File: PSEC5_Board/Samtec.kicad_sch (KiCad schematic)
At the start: 1 part, among them J1 QTH-040-01-X-D-DP-A

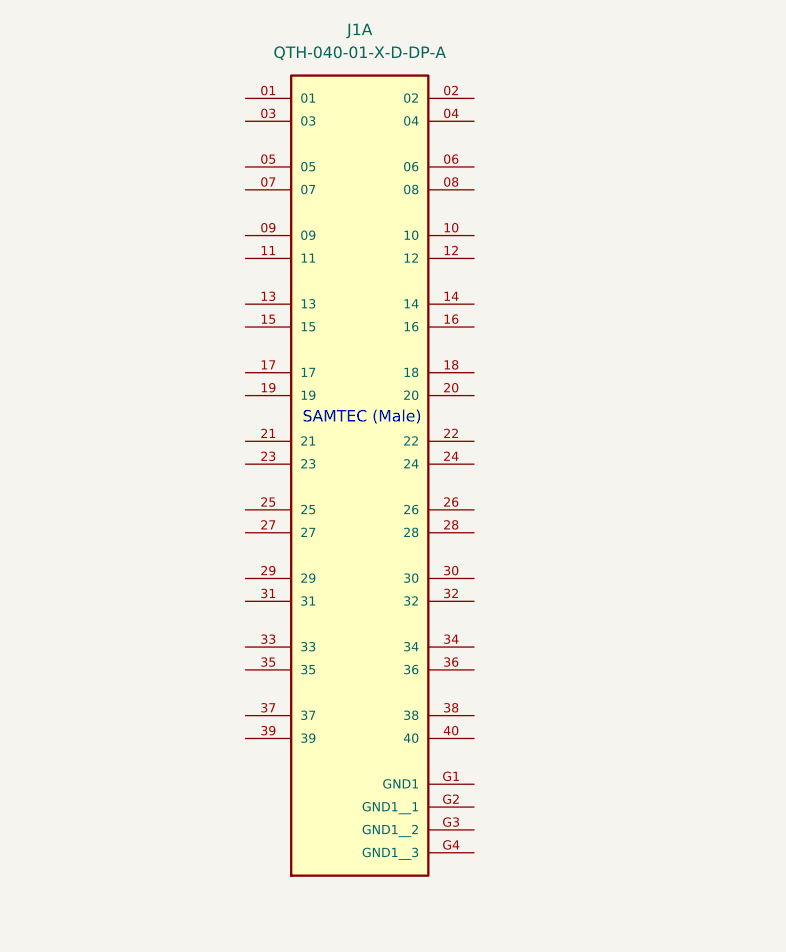
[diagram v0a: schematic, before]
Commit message: ctrl Board Schem, Updates to DUT
Uploaded all symobls for FPGA board to a ctrl_board schematic, as well as updated DUT board by adding labels to parts
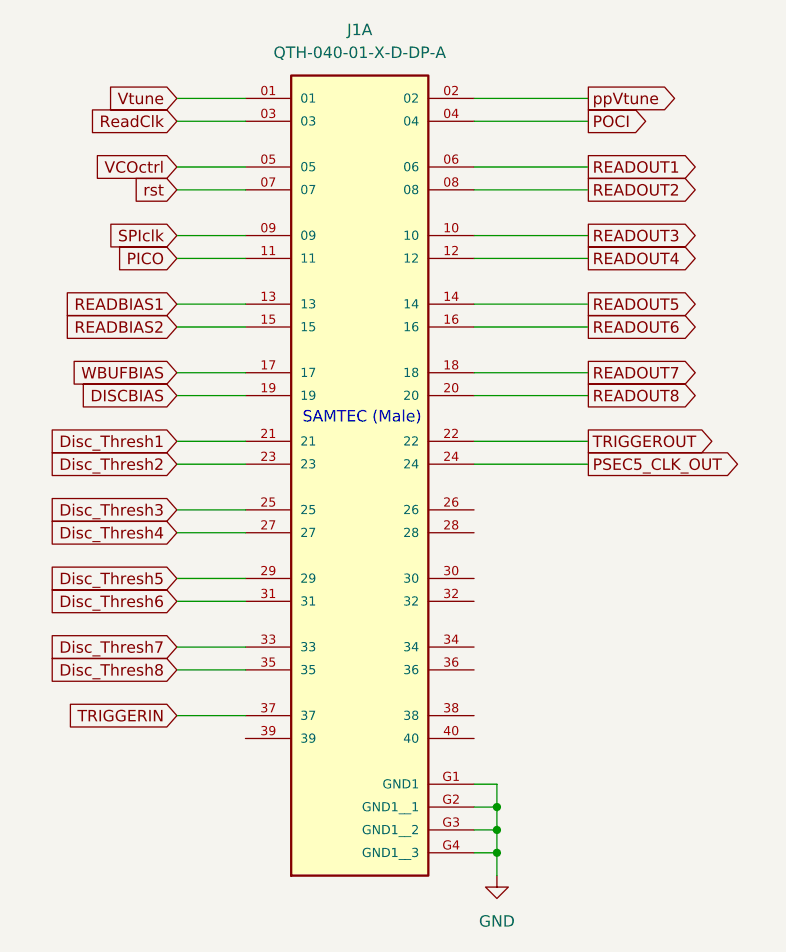
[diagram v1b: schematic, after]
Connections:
- net Vtune: now reaches J1.01
- net ppVtune: now reaches J1.02
- net ReadClk: now reaches J1.03
- net POCI: now reaches J1.04
- net VCOctrl: now reaches J1.05
- net READOUT1: now reaches J1.06
- net rst: now reaches J1.07
- net READOUT2: now reaches J1.08
- net SPIclk: now reaches J1.09
- net READOUT3: now reaches J1.10
- net PICO: now reaches J1.11
- net READOUT4: now reaches J1.12
- net READBIAS1: now reaches J1.13
- net READOUT5: now reaches J1.14
- net READBIAS2: now reaches J1.15
- net READOUT6: now reaches J1.16
- net WBUFBIAS: now reaches J1.17
- net READOUT7: now reaches J1.18
- net DISCBIAS: now reaches J1.19
- net READOUT8: now reaches J1.20
- net Disc_Thresh1: now reaches J1.21
- net TRIGGEROUT: now reaches J1.22
- net Disc_Thresh2: now reaches J1.23
- net PSEC5_CLK_OUT: now reaches J1.24
- net Disc_Thresh3: now reaches J1.25
- net Disc_Thresh4: now reaches J1.27
- net Disc_Thresh5: now reaches J1.29
- net Disc_Thresh6: now reaches J1.31
- net Disc_Thresh7: now reaches J1.33
- net Disc_Thresh8: now reaches J1.35
- net TRIGGERIN: now reaches J1.37
- net GND: now reaches J1.G1 (GND1)
- net GND: now also J1.G2 (GND1__1), J1.G3 (GND1__2), J1.G4 (GND1__3)

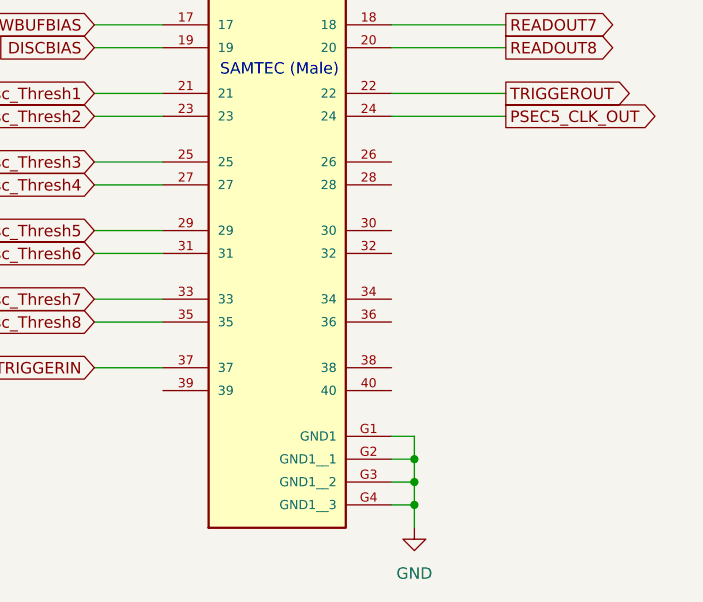
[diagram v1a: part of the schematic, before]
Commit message: Created Circuitry for Ad8332
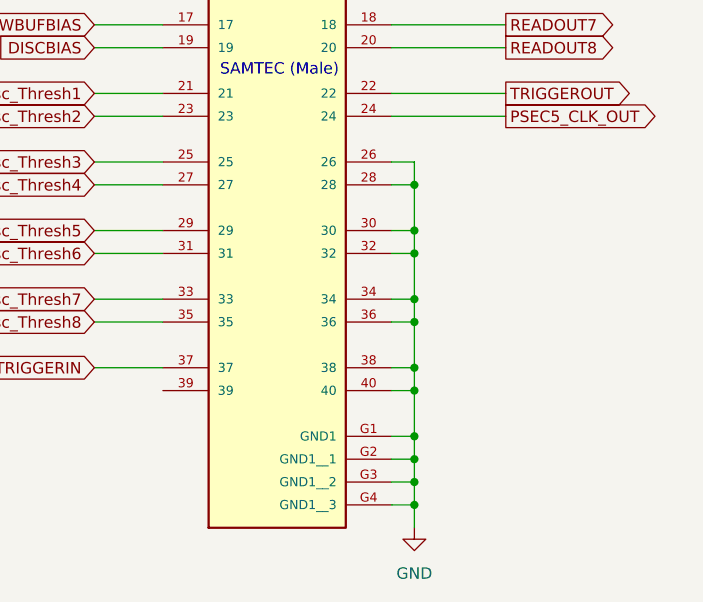
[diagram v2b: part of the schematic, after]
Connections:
- net GND: now also J1.26, J1.28, J1.30, J1.32, J1.34, J1.36, J1.38, J1.40
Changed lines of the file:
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@@
 	(paper "A4")
 	(junction
+		(at 80.01 95.25)
+		(diameter 0)
+		(color 0 0 0 0)
+	)
+	(junction
+		(at 80.01 118.11)
+		(diameter 0)
+		(color 0 0 0 0)
+	)
+	(junction
 		(at 80.01 128.27)
 		(diameter 0)
@@
 	)
 	(junction
+		(at 80.01 100.33)
+		(diameter 0)
+		(color 0 0 0 0)
+	)
+	(junction
+		(at 80.01 102.87)
+		(diameter 0)
+		(color 0 0 0 0)
+	)
+	(junction
+		(at 80.01 115.57)
+		(diameter 0)
+		(color 0 0 0 0)
+	)
+	(junction
 		(at 80.01 125.73)
 		(diameter 0)
@@
 	)
 	(junction
+		(at 80.01 123.19)
+		(diameter 0)
+		(color 0 0 0 0)
+	)
+	(junction
+		(at 80.01 107.95)
+		(diameter 0)
+		(color 0 0 0 0)
+	)
+	(junction
+		(at 80.01 110.49)
+		(diameter 0)
+		(color 0 0 0 0)
+	)
+	(junction
 		(at 80.01 130.81)
 		(diameter 0)
@@
 	(wire
 		(pts
+			(xy 80.01 102.87) (xy 80.01 100.33)
+		)
+		(stroke
+			(width 0)
+			(type default)
+		)
+	)
+	(wire
+		(pts
 			(xy 77.47 125.73) (xy 80.01 125.73)
 		)
@@
 	(wire
 		(pts
+			(xy 80.01 110.49) (xy 80.01 115.57)
+		)
+		(stroke
+			(width 0)
+			(type default)
+		)
+	)
+	(wire
+		(pts
 			(xy 44.45 64.77) (xy 52.07 64.77)
 		)
@@
 	(wire
 		(pts
+			(xy 77.47 110.49) (xy 80.01 110.49)
+		)
+		(stroke
+			(width 0)
+			(type default)
+		)
+	)
+	(wire
+		(pts
 			(xy 77.47 80.01) (xy 90.17 80.01)
 		)
@@
 	(wire
 		(pts
+			(xy 80.01 92.71) (xy 77.47 92.71)
+		)
+		(stroke
+			(width 0)
+			(type default)
+		)
+	)
+	(wire
+		(pts
 			(xy 44.45 85.09) (xy 52.07 85.09)
 		)
@@
 	(wire
 		(pts
+			(xy 77.47 95.25) (xy 80.01 95.25)
+		)
+		(stroke
+			(width 0)
+			(type default)
+		)
+	)
+	(wire
+		(pts
+			(xy 77.47 107.95) (xy 80.01 107.95)
+		)
+		(stroke
+			(width 0)
+			(type default)
+		)
+	)
+	(wire
+		(pts
 			(xy 77.47 62.23) (xy 90.17 62.23)
 		)
@@
 	(wire
 		(pts
+			(xy 80.01 115.57) (xy 80.01 118.11)
+		)
+		(stroke
+			(width 0)
+			(type default)
+		)
+	)
+	(wire
+		(pts
+			(xy 80.01 107.95) (xy 80.01 110.49)
+		)
+		(stroke
+			(width 0)
+			(type default)
+		)
+	)
+	(wire
+		(pts
+			(xy 77.47 100.33) (xy 80.01 100.33)
+		)
+		(stroke
+			(width 0)
+			(type default)
+		)
+	)
+	(wire
+		(pts
+			(xy 77.47 118.11) (xy 80.01 118.11)
+		)
+		(stroke
+			(width 0)
+			(type default)
+		)
+	)
+	(wire
+		(pts
 			(xy 44.45 46.99) (xy 52.07 46.99)
 		)
@@
 	(wire
 		(pts
+			(xy 80.01 100.33) (xy 80.01 95.25)
+		)
+		(stroke
+			(width 0)
+			(type default)
+		)
+	)
+	(wire
+		(pts
 			(xy 44.45 102.87) (xy 52.07 102.87)
 		)
@@
 	(wire
 		(pts
+			(xy 80.01 118.11) (xy 80.01 123.19)
+		)
+		(stroke
+			(width 0)
+			(type default)
+		)
+	)
+	(wire
+		(pts
 			(xy 80.01 130.81) (xy 80.01 133.35)
 		)
@@
 	(wire
 		(pts
+			(xy 80.01 95.25) (xy 80.01 92.71)
+		)
+		(stroke
+			(width 0)
+			(type default)
+		)
+	)
+	(wire
+		(pts
 			(xy 77.47 123.19) (xy 80.01 123.19)
 		)
@@
 	(wire
 		(pts
+			(xy 80.01 102.87) (xy 80.01 107.95)
+		)
+		(stroke
+			(width 0)
+			(type default)
+		)
+	)
+	(wire
+		(pts
 			(xy 44.45 57.15) (xy 52.07 57.15)
 		)
@@
 		)
 		(stroke
+			(width 0)
+			(type default)
+		)
+	)
+	(wire
+		(pts
+			(xy 77.47 102.87) (xy 80.01 102.87)
+		)
+		(stroke
+			(width 0)
+			(type default)
+		)
+	)
+	(wire
+		(pts
+			(xy 77.47 115.57) (xy 80.01 115.57)
+		)
+		(stroke

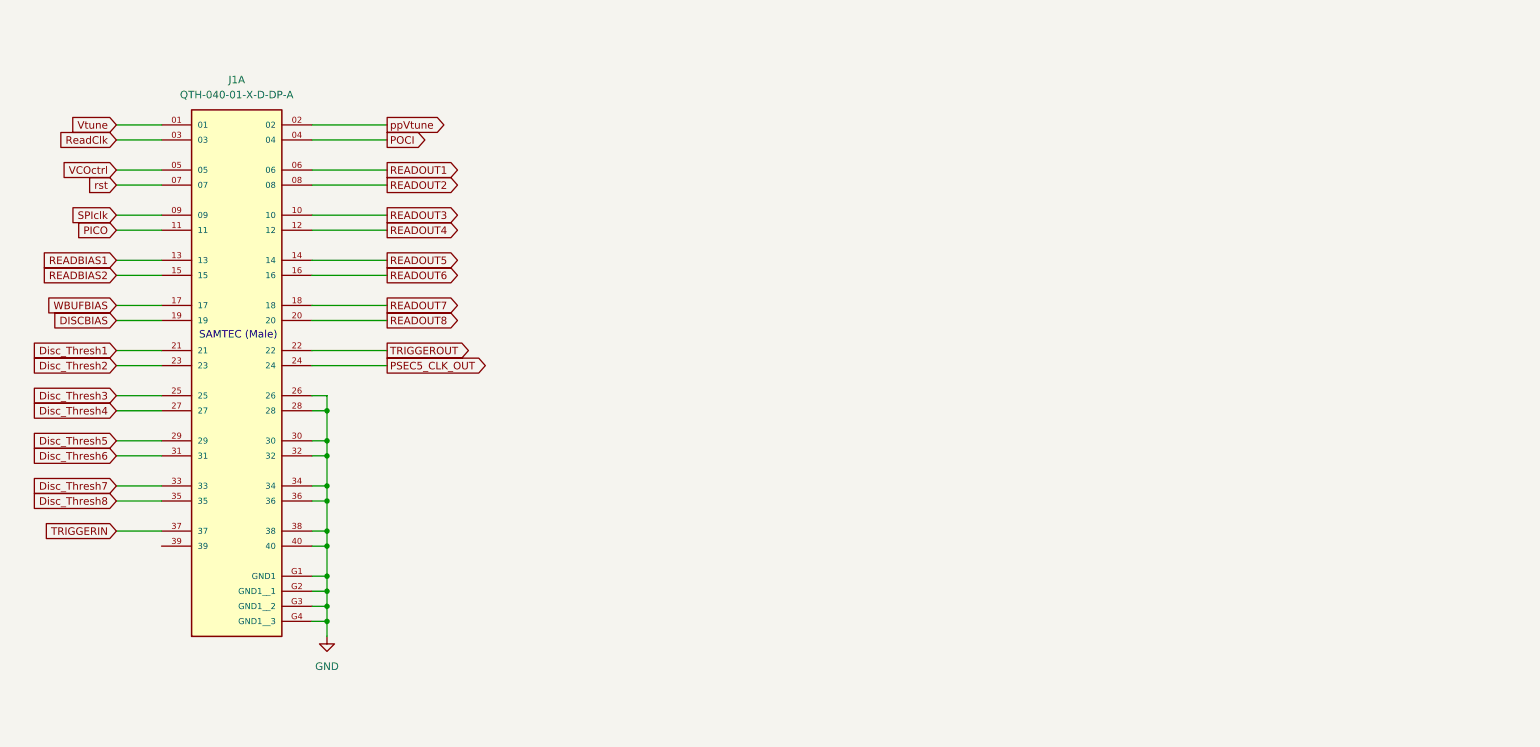
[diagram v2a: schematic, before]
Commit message: DUT Schematic Push
Very close -> Still need to convert to Sheet pins.

Added a second SAMTEC.
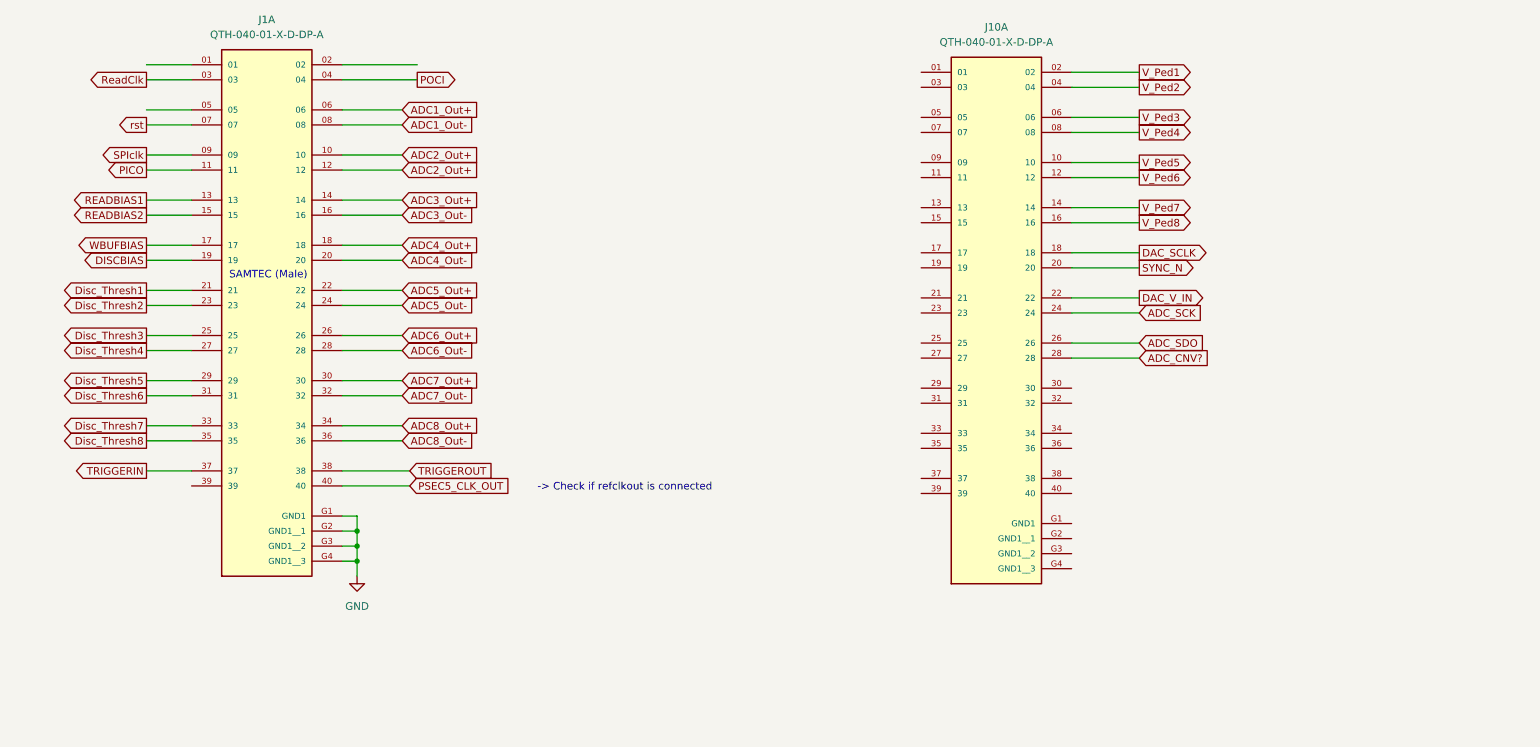
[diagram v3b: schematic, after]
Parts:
- added J10: QTH-040-01-X-D-DP-A, QTH-040-01-X-D-DP-A:SAMTEC_QTH-040-01-X-D-DP-A, symbol QTH-040-01-X-D-DP-A:QTH-040-01-X-D-DP-A
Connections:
- net READOUT4 is gone; now on net ADC2_Out+: J1.12
- net GND: no longer J1.26, J1.28, J1.30, J1.32, J1.34, J1.36, J1.38, J1.40
- net PSEC5_CLK_OUT: now also J1.40; no longer J1.24
- net TRIGGEROUT: now also J1.38; no longer J1.22
- net READOUT1 renamed ADC1_Out+
- net READOUT2 renamed ADC1_Out-
- net READOUT3 renamed ADC2_Out+
- net READOUT5 renamed ADC3_Out+
- net READOUT6 renamed ADC3_Out-
- net READOUT7 renamed ADC4_Out+
- net READOUT8 renamed ADC4_Out-
- net VCOctrl: no longer names the net of J1.05
- net Vtune: no longer names the net of J1.01
- net ppVtune: no longer names the net of J1.02
- new net ADC5_Out+: J1.22
- new net ADC5_Out-: J1.24
- new net ADC6_Out+: J1.26
- new net ADC6_Out-: J1.28
- new net ADC7_Out+: J1.30
- new net ADC7_Out-: J1.32
- new net ADC8_Out+: J1.34
- new net ADC8_Out-: J1.36
- new net ADC_CNV?: J10.28
- new net ADC_SCK: J10.24
- new net ADC_SDO: J10.26
- new net DAC_SCLK: J10.18
- new net DAC_V_IN: J10.22
- new net SYNC_N: J10.20
- new net V_Ped1: J10.02
- new net V_Ped2: J10.04
- new net V_Ped3: J10.06
- new net V_Ped4: J10.08
- new net V_Ped5: J10.10
- new net V_Ped6: J10.12
- new net V_Ped7: J10.14
- new net V_Ped8: J10.16
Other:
- note added: "-> Check if refclkout is connected"
- moved on the sheet: J1A

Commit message: DUT - Fixed ADC Driver
Passes ERC - SAMTEC connections still needs to be matched.
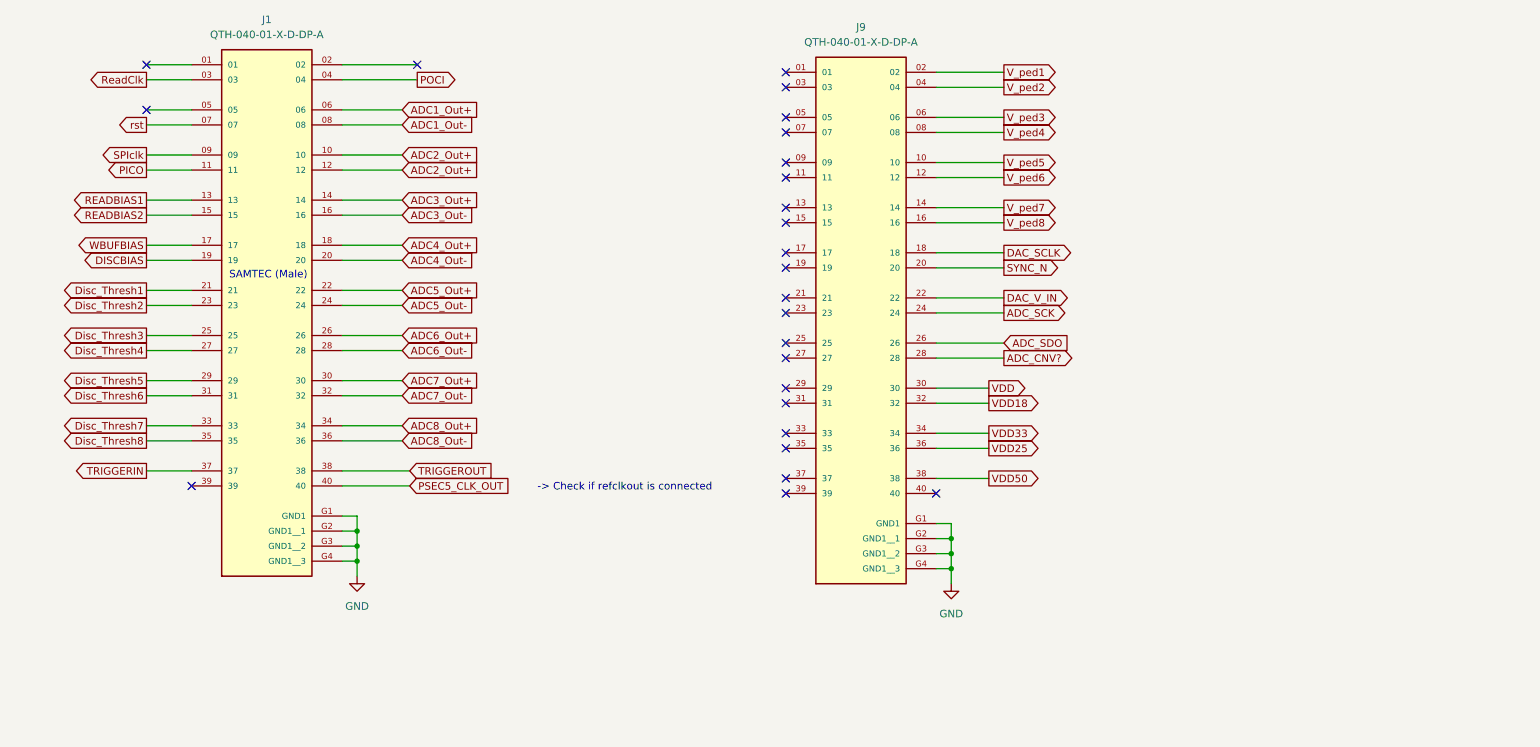
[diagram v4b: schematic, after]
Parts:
- removed J10: QTH-040-01-X-D-DP-A, QTH-040-01-X-D-DP-A:SAMTEC_QTH-040-01-X-D-DP-A, symbol QTH-040-01-X-D-DP-A:QTH-040-01-X-D-DP-A
- added J9: QTH-040-01-X-D-DP-A, QTH-040-01-X-D-DP-A:SAMTEC_QTH-040-01-X-D-DP-A, symbol QTH-040-01-X-D-DP-A:QTH-040-01-X-D-DP-A
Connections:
- net ADC_CNV?: now also J9.28
- net ADC_SCK: now also J9.24
- net ADC_SDO: now also J9.26
- net DAC_SCLK: now also J9.18
- net DAC_V_IN: now also J9.22
- net GND: now also J9.G1 (GND1), J9.G2 (GND1__1), J9.G3 (GND1__2), J9.G4 (GND1__3)
- net SYNC_N: now also J9.20
- new net VDD: J9.30
- new net VDD18: J9.32
- new net VDD25: J9.36
- new net VDD33: J9.34
- new net VDD50: J9.38
- new net V_ped1: J9.02
- new net V_ped2: J9.04
- new net V_ped3: J9.06
- new net V_ped4: J9.08
- new net V_ped5: J9.10
- new net V_ped6: J9.12
- new net V_ped7: J9.14
- new net V_ped8: J9.16
- no-connect marks 0 -> 25

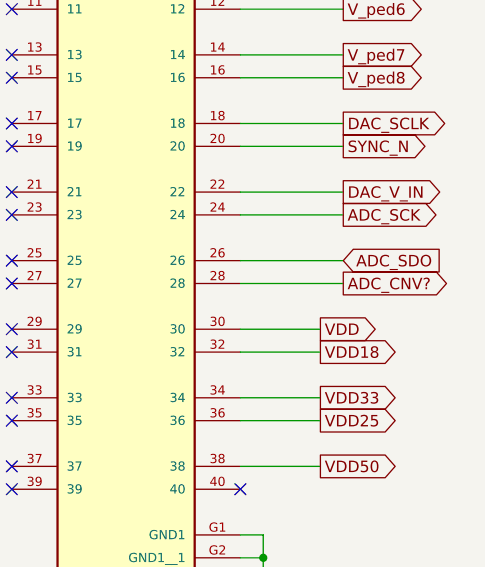
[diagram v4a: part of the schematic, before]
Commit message: DUT adjustments
New Nets in Layout,

Some name changes in Schematic
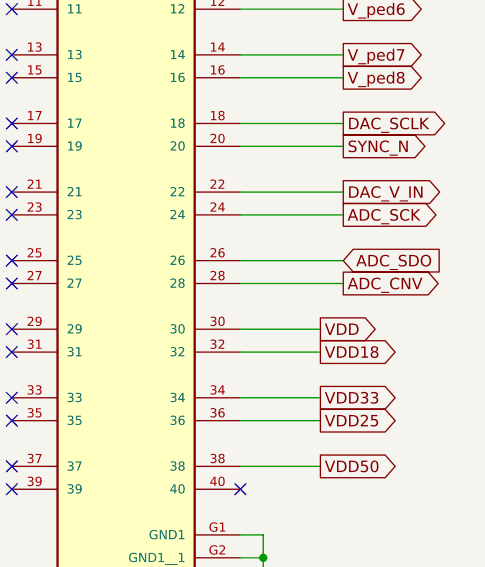
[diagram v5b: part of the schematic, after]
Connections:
- net ADC_CNV? renamed ADC_CNV
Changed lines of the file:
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@@
 		)
 	)
-	(global_label "ADC_CNV?"
+	(global_label "ADC_CNV"
 		(shape output)
 		(at 194.31 86.36 0)
